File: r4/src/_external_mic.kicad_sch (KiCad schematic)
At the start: 134 parts, among them Q12 BSS84PW, Q13 BSS84PW, Q14 NX6008NBKW, Q15 NX3008NBKW, Q16 NX3008NBKW, Q17 NX3008NBKW, Q18 NX3008NBKW, Q19 NX3008NBKW, Q20 BSS84PW, Q21 BSS84PW, Q22 NX3008NBKW, Q23 NX3008NBKW, Q24 NX3008NBKW, Q25 BSS84PW, T18 , T19 , T20 , T23 , T24 , T25 , T26 , T27 , T28 , T29 , T30 , T31 , T32 , T33 , T34 , T35 , T36 , T37 , T38 , T43 , T44 , T45 , T46 , T47 , T48 , T49 , T50 , U17 74HC20, U18 THAT5173, U19 74HC74, U20 74HC132, U21 74HC4520, U22 74HC132, U23 THAT1580, U24 74HC688, U25 LM4562, U26 74HC688, U27 AD4005

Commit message: Remove duplicate testpoint
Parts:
- removed T36: (no value), TestPoint:TestPoint_Pad_D1.0mm, symbol Connector:TestPoint
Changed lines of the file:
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@@
   (junction (at 410.21 312.42) (diameter 0) (color 0 0 0 0)
   )
-  (junction (at 554.99 311.15) (diameter 0) (color 0 0 0 0)
-  )
   (junction (at 113.03 21.59) (diameter 0) (color 0 0 0 0)
   )
@@
     (stroke (width 0) (type default))
   )
-  (wire (pts (xy 554.99 311.15) (xy 554.99 314.96))
-    (stroke (width 0) (type default))
-  )
   (wire (pts (xy 393.7 326.39) (xy 393.7 344.17))
     (stroke (width 0) (type default))
@@
     (stroke (width 0) (type default))
   )
-  (wire (pts (xy 544.83 311.15) (xy 554.99 311.15))
+  (wire (pts (xy 544.83 311.15) (xy 557.53 311.15))
     (stroke (width 0) (type default))
   )
@@
     (stroke (width 0) (type default))
   )
-  (wire (pts (xy 554.99 311.15) (xy 557.53 311.15))
-    (stroke (width 0) (type default))
-  )
   (wire (pts (xy 294.64 351.79) (xy 306.07 351.79))
     (stroke (width 0) (type default))
@@
         )
       )
-    )
-  )
-  (symbol (lib_id "Connector:TestPoint") (at 554.99 314.96 0) (mirror x) (unit 1)
-    (in_bom yes) (on_board yes) (dnp no)
-    (property "Reference" "T36" (at 554.99 320.04 90)
-      (effects (font (size 1.27 1.27)) (justify left))
-    )
-    (property "Value" " " (at 556.26 320.04 90)
-      (effects (font (size 1.27 1.27)) (justify left))
-    )
-    (property "Footprint" "TestPoint:TestPoint_Pad_D1.0mm" (at 560.07 314.96 0)
-      (effects (font (size 1.27 1.27)) hide)
-    )
-    (property "Datasheet" "~" (at 560.07 314.96 0)
-      (effects (font (size 1.27 1.27)) hide)
-    )
-    (pin "1")
-    (instances
-      (project "bugg-main-r4"
-        (path "/e3eb514f-6ce4-4abe-ba20-f82f0015628f/41f15edd-4583-4f5d-8a81-daeb7c83b416"
-          (reference "T36") (unit 1) (value " ") (footprint "TestPoint:TestPoint_Pad_D1.0mm")
-        )
-      )

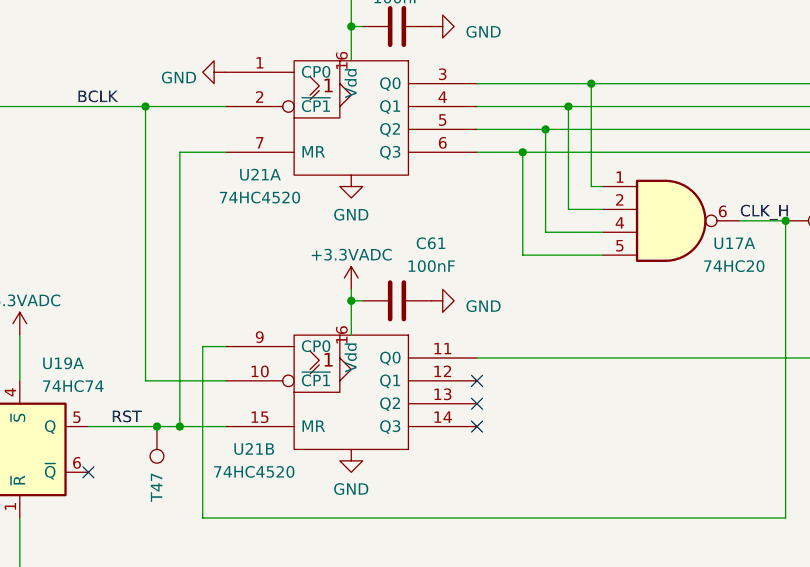
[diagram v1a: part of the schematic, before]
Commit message: Remove dupicate decoupling cap on U21
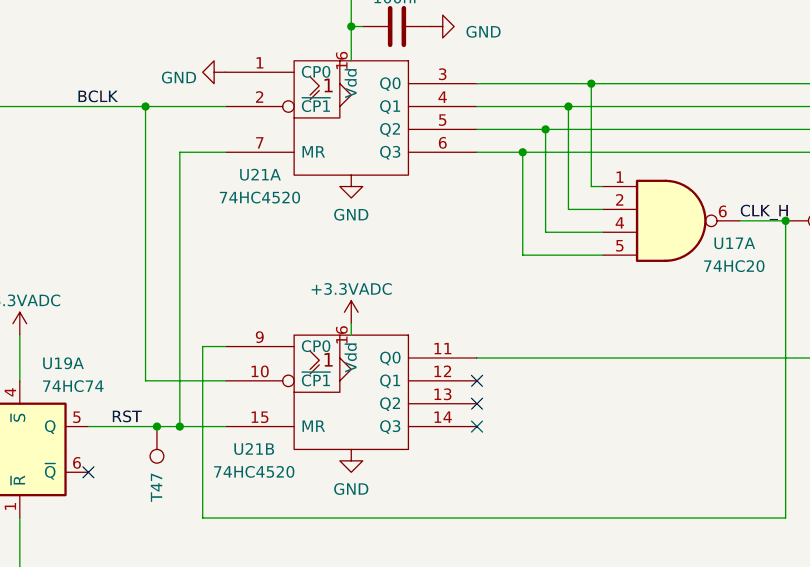
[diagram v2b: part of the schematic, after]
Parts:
- removed C61: 100nF, Capacitor_SMD:C_0402_1005Metric, symbol Device:C
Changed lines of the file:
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@@
   (junction (at 161.29 234.95) (diameter 0) (color 0 0 0 0)
   )
-  (junction (at 287.02 99.06) (diameter 0) (color 0 0 0 0)
-  )
   (junction (at 278.13 220.98) (diameter 0) (color 0 0 0 0)
   )
@@
     (stroke (width 0) (type default))
   )
-  (wire (pts (xy 287.02 99.06) (xy 288.29 99.06))
-    (stroke (width 0) (type default))
-  )
   (wire (pts (xy 473.71 314.96) (xy 480.06 314.96))
     (stroke (width 0) (type default))
@@
     (stroke (width 0) (type default))
   )
-  (wire (pts (xy 287.02 97.79) (xy 287.02 99.06))
-    (stroke (width 0) (type default))
-  )
   (wire (pts (xy 266.7 234.95) (xy 270.51 234.95))
     (stroke (width 0) (type default))
@@
     (stroke (width 0) (type default))
   )
-  (wire (pts (xy 287.02 99.06) (xy 287.02 102.87))
+  (wire (pts (xy 287.02 101.6) (xy 287.02 102.87))
     (stroke (width 0) (type default))
   )
@@
     )
   )
-  (symbol (lib_id "Device:C") (at 292.1 99.06 270) (mirror x) (unit 1)
-    (in_bom yes) (on_board yes) (dnp no)
-    (property "Reference" "C61" (at 295.91 92.71 90)
-      (effects (font (size 1.27 1.27)))
-    )
-    (property "Value" "100nF" (at 295.91 95.25 90)
-      (effects (font (size 1.27 1.27)))
-    )
-    (property "Footprint" "Capacitor_SMD:C_0402_1005Metric" (at 288.29 98.0948 0)
-      (effects (font (size 1.27 1.27)) hide)
-    )
-    (property "Datasheet" "~" (at 292.1 99.06 0)
-      (effects (font (size 1.27 1.27)) hide)
-    )
-    (pin "1")
-    (pin "2")
-    (instances
-      (project "bugg-main-r4"
-        (path "/e3eb514f-6ce4-4abe-ba20-f82f0015628f/41f15edd-4583-4f5d-8a81-daeb7c83b416"
-          (reference "C61") (unit 1) (value "100nF") (footprint "Capacitor_SMD:C_0402_1005Metric")
-        )
-      )
-    )
-  )
   (symbol (lib_id "power:GNDA") (at 91.44 261.62 0) (unit 1)
     (in_bom yes) (on_board yes) (dnp no)
@@
     )
   )
-  (symbol (lib_id "power:+3.3VADC") (at 287.02 97.79 0) (unit 1)
+  (symbol (lib_id "power:+3.3VADC") (at 287.02 101.6 0) (unit 1)
     (in_bom yes) (on_board yes) (dnp no) (fields_autoplaced)
-    (property "Reference" "#PWR0266" (at 290.83 99.06 0)
+    (property "Reference" "#PWR0266" (at 290.83 102.87 0)
       (effects (font (size 1.27 1.27)) hide)
     )
-    (property "Value" "+3.3VADC" (at 287.02 93.98 0)
+    (property "Value" "+3.3VADC" (at 287.02 97.79 0)
       (effects (font (size 1.27 1.27)))
     )
-    (property "Footprint" "" (at 287.02 97.79 0)
+    (property "Footprint" "" (at 287.02 101.6 0)
       (effects (font (size 1.27 1.27)) hide)
     )
-    (property "Datasheet" "" (at 287.02 97.79 0)
+    (property "Datasheet" "" (at 287.02 101.6 0)
       (effects (font (size 1.27 1.27)) hide)
     )
@@
         )
       )
-    )
-  )
-  (symbol (lib_id "power:GND") (at 295.91 99.06 90) (unit 1)
-    (in_bom yes) (on_board yes) (dnp no) (fields_autoplaced)
-    (property "Reference" "#PWR0158" (at 302.26 99.06 0)
-      (effects (font (size 1.27 1.27)) hide)
-    )
-    (property "Value" "GND" (at 299.72 99.695 90)
-      (effects (font (size 1.27 1.27)) (justify right))
-    )
-    (property "Footprint" "" (at 295.91 99.06 0)
-      (effects (font (size 1.27 1.27)) hide)
-    )
-    (property "Datasheet" "" (at 295.91 99.06 0)
-      (effects (font (size 1.27 1.27)) hide)
-    )
-    (pin "1")
-    (instances
-      (project "bugg-main-r4"
-        (path "/e3eb514f-6ce4-4abe-ba20-f82f0015628f/41f15edd-4583-4f5d-8a81-daeb7c83b416"
-          (reference "#PWR0158") (unit 1) (value "GND") (footprint "")
-        )
-      )

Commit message: Remove dupicate decoupling cap on U18
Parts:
- removed C51: 100nF, Capacitor_SMD:C_0402_1005Metric, symbol Device:C
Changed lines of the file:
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@@
   (junction (at 436.88 351.79) (diameter 0) (color 0 0 0 0)
   )
-  (junction (at 191.77 105.41) (diameter 0) (color 0 0 0 0)
-  )
   (junction (at 217.17 335.28) (diameter 0) (color 0 0 0 0)
   )
@@
     (stroke (width 0) (type default))
   )
-  (wire (pts (xy 191.77 105.41) (xy 194.31 105.41))
-    (stroke (width 0) (type default))
-  )
   (wire (pts (xy 278.13 209.55) (xy 278.13 210.82))
     (stroke (width 0) (type default))
@@
     (stroke (width 0) (type default))
   )
-  (wire (pts (xy 191.77 105.41) (xy 191.77 115.57))
+  (wire (pts (xy 191.77 111.76) (xy 191.77 115.57))
     (stroke (width 0) (type default))
   )
@@
     (stroke (width 0) (type default))
   )
-  (wire (pts (xy 191.77 102.87) (xy 191.77 105.41))
-    (stroke (width 0) (type default))
-  )
   (wire (pts (xy 321.31 295.91) (xy 330.2 295.91))
     (stroke (width 0) (type default))
@@
     )
   )
-  (symbol (lib_id "power:+3.3VADC") (at 191.77 102.87 0) (unit 1)
+  (symbol (lib_id "power:+3.3VADC") (at 191.77 111.76 0) (unit 1)
     (in_bom yes) (on_board yes) (dnp no) (fields_autoplaced)
-    (property "Reference" "#PWR0213" (at 195.58 104.14 0)
+    (property "Reference" "#PWR0213" (at 195.58 113.03 0)
       (effects (font (size 1.27 1.27)) hide)
     )
-    (property "Value" "+3.3VADC" (at 191.77 99.06 0)
+    (property "Value" "+3.3VADC" (at 191.77 107.95 0)
       (effects (font (size 1.27 1.27)))
     )
-    (property "Footprint" "" (at 191.77 102.87 0)
+    (property "Footprint" "" (at 191.77 111.76 0)
       (effects (font (size 1.27 1.27)) hide)
     )
-    (property "Datasheet" "" (at 191.77 102.87 0)
+    (property "Datasheet" "" (at 191.77 111.76 0)
       (effects (font (size 1.27 1.27)) hide)
     )
@@
     )
   )
-  (symbol (lib_id "Device:C") (at 198.12 105.41 270) (mirror x) (unit 1)
-    (in_bom yes) (on_board yes) (dnp no)
-    (property "Reference" "C51" (at 200.66 99.06 90)
-      (effects (font (size 1.27 1.27)))
-    )
-    (property "Value" "100nF" (at 200.66 101.6 90)
-      (effects (font (size 1.27 1.27)))
-    )
-    (property "Footprint" "Capacitor_SMD:C_0402_1005Metric" (at 194.31 104.4448 0)
-      (effects (font (size 1.27 1.27)) hide)
-    )
-    (property "Datasheet" "~" (at 198.12 105.41 0)
-      (effects (font (size 1.27 1.27)) hide)
-    )
-    (pin "1")
-    (pin "2")
-    (instances
-      (project "bugg-main-r4"
-        (path "/e3eb514f-6ce4-4abe-ba20-f82f0015628f/41f15edd-4583-4f5d-8a81-daeb7c83b416"
-          (reference "C51") (unit 1) (value "100nF") (footprint "Capacitor_SMD:C_0402_1005Metric")
-        )
-      )
-    )
-  )
   (symbol (lib_id "Device:R") (at 521.97 114.3 90) (unit 1)
     (in_bom yes) (on_board yes) (dnp no)
@@
         )
       )
-    )
-  )
-  (symbol (lib_id "power:GND") (at 201.93 105.41 90) (unit 1)
-    (in_bom yes) (on_board yes) (dnp no) (fields_autoplaced)
-    (property "Reference" "#PWR079" (at 208.28 105.41 0)
-      (effects (font (size 1.27 1.27)) hide)
-    )
-    (property "Value" "GND" (at 205.74 106.045 90)
-      (effects (font (size 1.27 1.27)) (justify right))
-    )
-    (property "Footprint" "" (at 201.93 105.41 0)
-      (effects (font (size 1.27 1.27)) hide)
-    )
-    (property "Datasheet" "" (at 201.93 105.41 0)
-      (effects (font (size 1.27 1.27)) hide)
-    )
-    (pin "1")
-    (instances
-      (project "bugg-main-r4"
-        (path "/e3eb514f-6ce4-4abe-ba20-f82f0015628f/41f15edd-4583-4f5d-8a81-daeb7c83b416"
-          (reference "#PWR079") (unit 1) (value "GND") (footprint "")
-        )
-      )

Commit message: Add ferrite to 5173 digital supply
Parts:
- added FB3: 1k@100MHz, Inductor_SMD:L_0603_1608Metric, symbol Device:FerriteBead_Small
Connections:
- net +3.3VADC: now also FB3.2; no longer C52.2, U18.11 (VDD)
- new net: C52.2, FB3.1, U18.11 (VDD)
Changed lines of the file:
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@@
     (stroke (width 0) (type default))
   )
-  (wire (pts (xy 191.77 111.76) (xy 191.77 115.57))
-    (stroke (width 0) (type default))
-  )
   (wire (pts (xy 342.9 302.26) (xy 347.98 302.26))
     (stroke (width 0) (type default))
@@
     (stroke (width 0) (type default))
   )
+  (wire (pts (xy 191.77 109.22) (xy 191.77 115.57))
+    (stroke (width 0) (type default))
+  )
   (wire (pts (xy 393.7 326.39) (xy 440.69 326.39))
     (stroke (width 0) (type default))
@@
     )
   )
+  (symbol (lib_id "Device:FerriteBead_Small") (at 191.77 106.68 0) (mirror x) (unit 1)
+    (in_bom yes) (on_board yes) (dnp no)
+    (property "Reference" "FB3" (at 189.23 106.0831 0)
+      (effects (font (size 1.27 1.27)) (justify right))
+    )
+    (property "Value" "1k@100MHz" (at 189.23 108.6231 0)
+      (effects (font (size 1.27 1.27)) (justify right))
+    )
+    (property "Footprint" "Inductor_SMD:L_0603_1608Metric" (at 189.992 106.68 90)
+      (effects (font (size 1.27 1.27)) hide)
+    )
+    (property "Datasheet" "~" (at 191.77 106.68 0)
+      (effects (font (size 1.27 1.27)) hide)
+    )
+    (pin "1")
+    (pin "2")
+    (instances
+      (project "bugg-main-r4"
+        (path "/e3eb514f-6ce4-4abe-ba20-f82f0015628f/e93db74d-0429-4e7f-b256-c16b4c3a83e7"
+          (reference "FB3") (unit 1) (value "1k@100MHz") (footprint "Inductor_SMD:L_0603_1608Metric")
+        )
+        (path "/e3eb514f-6ce4-4abe-ba20-f82f0015628f/41f15edd-4583-4f5d-8a81-daeb7c83b416"
+          (reference "FB7") (unit 1) (value "1k@100MHz") (footprint "Inductor_SMD:L_0603_1608Metric")
+        )
+      )
+    )
+  )
   (symbol (lib_id "Connector:TestPoint") (at 212.09 134.62 270) (unit 1)
     (in_bom yes) (on_board yes) (dnp no)
@@
     )
   )
-  (symbol (lib_id "power:+3.3VADC") (at 191.77 111.76 0) (unit 1)
+  (symbol (lib_id "power:+3.3VADC") (at 191.77 104.14 0) (unit 1)
     (in_bom yes) (on_board yes) (dnp no) (fields_autoplaced)
-    (property "Reference" "#PWR0213" (at 195.58 113.03 0)
+    (property "Reference" "#PWR0213" (at 195.58 105.41 0)
       (effects (font (size 1.27 1.27)) hide)
     )
-    (property "Value" "+3.3VADC" (at 191.77 107.95 0)
+    (property "Value" "+3.3VADC" (at 191.77 100.33 0)
       (effects (font (size 1.27 1.27)))
     )
-    (property "Footprint" "" (at 191.77 111.76 0)
+    (property "Footprint" "" (at 191.77 104.14 0)
       (effects (font (size 1.27 1.27)) hide)
     )
-    (property "Datasheet" "" (at 191.77 111.76 0)
+    (property "Datasheet" "" (at 191.77 104.14 0)
       (effects (font (size 1.27 1.27)) hide)
     )

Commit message: ERC pass. A few errors remain but they are impossible to fix.
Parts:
- U23: symbol Audio:THAT1580 -> j_Audio:THAT1580
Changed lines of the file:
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@@
   (junction (at 396.24 312.42) (diameter 0) (color 0 0 0 0)
   )
+  (junction (at 191.77 111.76) (diameter 0) (color 0 0 0 0)
+  )
   (junction (at 340.36 323.85) (diameter 0) (color 0 0 0 0)
   )
@@
     (stroke (width 0) (type default))
   )
+  (wire (pts (xy 191.77 111.76) (xy 191.77 115.57))
+    (stroke (width 0) (type default))
+  )
   (wire (pts (xy 542.29 311.15) (xy 544.83 311.15))
     (stroke (width 0) (type default))
@@
     (stroke (width 0) (type default))
   )
-  (wire (pts (xy 191.77 109.22) (xy 191.77 115.57))
+  (wire (pts (xy 191.77 109.22) (xy 191.77 111.76))
     (stroke (width 0) (type default))
   )
@@
     )
   )
+  (symbol (lib_id "power:PWR_FLAG") (at 191.77 111.76 270) (unit 1)
+    (in_bom yes) (on_board yes) (dnp no) (fields_autoplaced)
+    (property "Reference" "#FLG0115" (at 193.675 111.76 0)
+      (effects (font (size 1.27 1.27)) hide)
+    )
+    (property "Value" "PWR_FLAG" (at 195.58 112.395 90)
+      (effects (font (size 1.27 1.27)) (justify left) hide)
+    )
+    (property "Footprint" "" (at 191.77 111.76 0)
+      (effects (font (size 1.27 1.27)) hide)
+    )
+    (property "Datasheet" "~" (at 191.77 111.76 0)
+      (effects (font (size 1.27 1.27)) hide)
+    )
+    (pin "1")
+    (instances
+      (project "bugg-main-r4"
+        (path "/e3eb514f-6ce4-4abe-ba20-f82f0015628f/41f15edd-4583-4f5d-8a81-daeb7c83b416"
+          (reference "#FLG0115") (unit 1) (value "PWR_FLAG") (footprint "")
+        )
+      )
+    )
+  )
   (symbol (lib_id "Device:C") (at 138.43 35.56 0) (mirror x) (unit 1)
     (in_bom yes) (on_board yes) (dnp no) (fields_autoplaced)
@@
     )
   )
-  (symbol (lib_id "Audio:THAT1580") (at 342.9 335.28 0) (unit 1)
+  (symbol (lib_id "j_Audio:THAT1580") (at 342.9 335.28 0) (unit 1)
     (in_bom yes) (on_board yes) (dnp no)
     (property "Reference" "U23" (at 342.9 326.39 0)
@@
       (effects (font (size 1.27 1.27)) (justify left))
     )
-    (property "Footprint" "Package_DFN_QFN:QFN-16-1EP_4x4mm_P0.65mm_EP2.1x2.1mm_ThermalVias" (at 342.9 335.28 0)
+    (property "Footprint" "Package_DFN_QFN:QFN-16-1EP_4x4mm_P0.65mm_EP2.1x2.1mm_ThermalVias" (at 342.9 309.88 0)
       (effects (font (size 1.27 1.27)) hide)
     )
-    (property "Datasheet" "http://www.thatcorp.com/datashts/THAT_1580_Datasheet.pdf" (at 342.9 335.28 0)
+    (property "Datasheet" "http://www.thatcorp.com/datashts/THAT_1580_Datasheet.pdf" (at 335.28 312.42 0)
       (effects (font (size 1.27 1.27)) hide)
     )
+    (pin "1")
+    (pin "11")
+    (pin "14")
+    (pin "16")
+    (pin "4")
+    (pin "5")
+    (pin "8")
+    (pin "9")
     (pin "10")
     (pin "12")

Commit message: Add thermal vias to 1573
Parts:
- U18: footprint Package_DFN_QFN:QFN-24-1EP_5x5mm_P0.65mm_EP3.4x3.4mm -> Package_DFN_QFN:QFN-24-1EP_5x5mm_P0.65mm_EP3.4x3.4mm_ThermalVias
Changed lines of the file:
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@@
       (effects (font (size 1.27 1.27)) (justify right))
     )
-    (property "Footprint" "Package_DFN_QFN:QFN-24-1EP_5x5mm_P0.65mm_EP3.4x3.4mm" (at 340.36 285.75 0)
+    (property "Footprint" "Package_DFN_QFN:QFN-24-1EP_5x5mm_P0.65mm_EP3.4x3.4mm_ThermalVias" (at 340.36 285.75 0)
       (effects (font (size 1.27 1.27)) hide)
     )
@@
       (project "bugg-main-r4"
         (path "/e3eb514f-6ce4-4abe-ba20-f82f0015628f/41f15edd-4583-4f5d-8a81-daeb7c83b416"
-          (reference "U18") (unit 1) (value "THAT5173") (footprint "Package_DFN_QFN:QFN-24-1EP_5x5mm_P0.65mm_EP3.4x3.4mm")
+          (reference "U18") (unit 1) (value "THAT5173") (footprint "Package_DFN_QFN:QFN-24-1EP_5x5mm_P0.65mm_EP3.4x3.4mm_ThermalVias")
         )
       )
@@
       (effects (font (size 1.27 1.27)) (justify right))
     )
-    (property "Footprint" "Package_DFN_QFN:QFN-24-1EP_5x5mm_P0.65mm_EP3.4x3.4mm" (at 191.77 132.08 0)
+    (property "Footprint" "Package_DFN_QFN:QFN-24-1EP_5x5mm_P0.65mm_EP3.4x3.4mm_ThermalVias" (at 191.77 132.08 0)
       (effects (font (size 1.27 1.27)) hide)
     )
@@
       (project "bugg-main-r4"
         (path "/e3eb514f-6ce4-4abe-ba20-f82f0015628f/41f15edd-4583-4f5d-8a81-daeb7c83b416"
-          (reference "U18") (unit 2) (value "THAT5173") (footprint "Package_DFN_QFN:QFN-24-1EP_5x5mm_P0.65mm_EP3.4x3.4mm")
-        )
-      )
+          (reference "U18") (unit 2) (value "THAT5173") (footprint "Package_DFN_QFN:QFN-24-1EP_5x5mm_P0.65mm_EP3.4x3.4mm_ThermalVias")
+        )
+      )

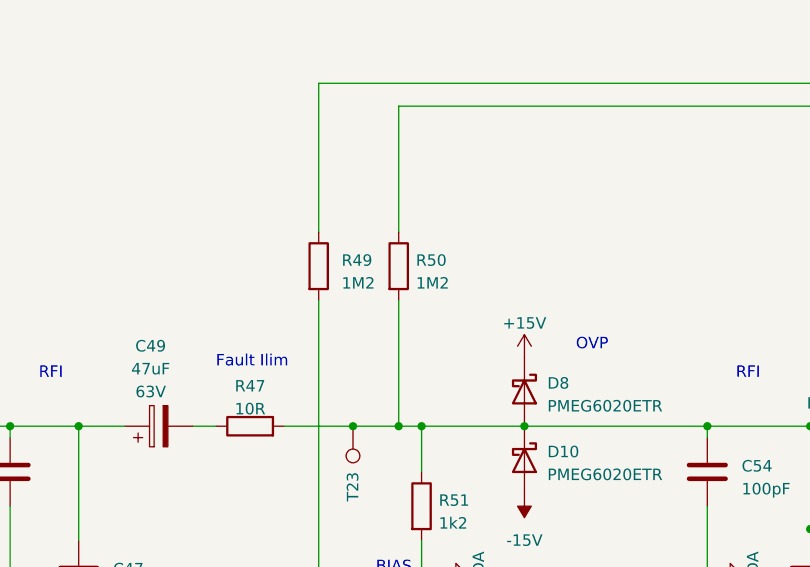
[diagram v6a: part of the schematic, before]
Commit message: Change 1.2M servo resistors to 1.3M to save a BOM line
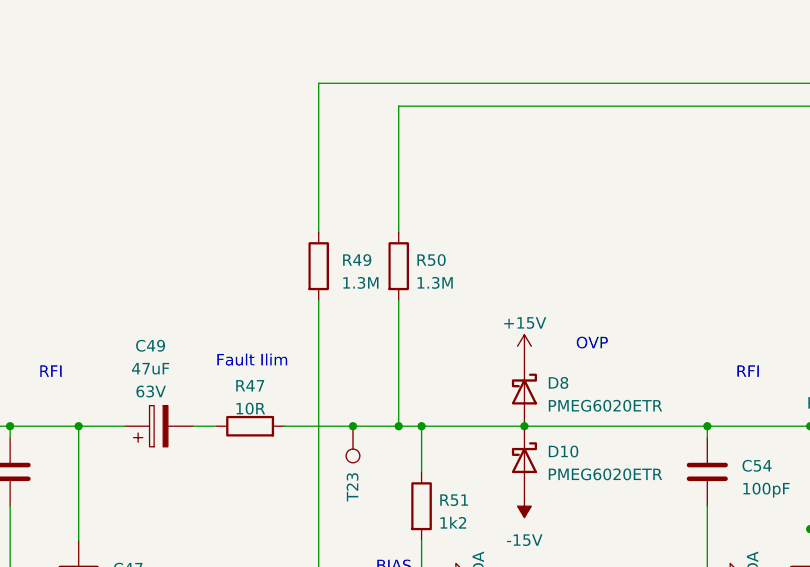
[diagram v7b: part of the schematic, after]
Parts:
- R49, R50: value 1M2 -> 1.3M
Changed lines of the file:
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@@
       (effects (font (size 1.27 1.27)) (justify left))
     )
-    (property "Value" "1M2" (at 254 302.895 0)
+    (property "Value" "1.3M" (at 254 302.895 0)
       (effects (font (size 1.27 1.27)) (justify left))
     )
@@
       (project "bugg-main-r4"
         (path "/e3eb514f-6ce4-4abe-ba20-f82f0015628f/41f15edd-4583-4f5d-8a81-daeb7c83b416"
-          (reference "R49") (unit 1) (value "1M2") (footprint "Resistor_SMD:R_0402_1005Metric")
+          (reference "R49") (unit 1) (value "1.3M") (footprint "Resistor_SMD:R_0402_1005Metric")
         )
       )
@@
       (effects (font (size 1.27 1.27)) (justify left))
     )
-    (property "Value" "1M2" (at 262.255 302.895 0)
+    (property "Value" "1.3M" (at 262.255 302.895 0)
       (effects (font (size 1.27 1.27)) (justify left))
     )
@@
       (project "bugg-main-r4"
         (path "/e3eb514f-6ce4-4abe-ba20-f82f0015628f/41f15edd-4583-4f5d-8a81-daeb7c83b416"
-          (reference "R50") (unit 1) (value "1M2") (footprint "Resistor_SMD:R_0402_1005Metric")
-        )
-      )
+          (reference "R50") (unit 1) (value "1.3M") (footprint "Resistor_SMD:R_0402_1005Metric")
+        )
+      )
